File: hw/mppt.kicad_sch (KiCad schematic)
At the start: 11 parts

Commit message: hw changes
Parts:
- TJ302, TJ303: footprint mppt:1225_SMD -> footprints:1225_SMD
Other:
- moved on the sheet: TJ302, TJ303

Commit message: v0.2.0
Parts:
- removed TJ302 (x2): Thermal Jumper, Resistor_SMD:R_0805_2012Metric, symbol Jumper:SolderJumper_2_Bridged
- removed TJ302, TJ303: Thermal Jumper, footprints:1225_SMD, symbol Jumper:SolderJumper_2_Bridged
- H101, H102, H103, H104: footprint MountingHole:MountingHole_3.5mm -> MountingHole:MountingHole_3.2mm_M3
- TJ303: footprint footprints:1225_SMD -> footprints:vishay_THJP1225ABT1; Cost 2.60 -> 2.03; P/N 71-THJP1225AST1 -> THJP1225ABT1
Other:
- added sheet comm_can (comm_can.kicad_sch)
- sheet controller ports: added CAN_RX, CAN_TX; removed none
- note added: "v0.1.1 - Fix for BNC footprint swapping signal and ground. - Fix for OPA990 footprint, rotating three pins. - Fix for mislabeling 1uF 2220 switching cap. This should be 2.2uF. - Fix for bad ground isolation for current sensors. - Fix for ERROR LED being hooked up to USB_DP and CAN1_TD pin. v0.2.0rc (summer array testing) - Revised component symbol->footprint->model listings. - Updated component s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"
- note added: "v0.2.0rc"
- note removed: "v0.1.1rc"
- note removed: "v0.1.1rc - Fix for BNC footprint swapping signal and ground. - Fix for OPA990 footprint, rotating three pins. - Fix for mislabeling 1uF 2220 switching cap. This should be 2.2uF. - Fix for bad ground isolation for current sensors. - Fix for ERROR LED being hooked up to USB_DP and CAN1_TD pin. v0.2.0 (summer array testing) - Swap mounting holes to M3. - Add I/O power fuse. - Add HF low uF caps on I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"
- company: UT LHR Solar -> LHR Solar
- moved on the sheet: TJ303

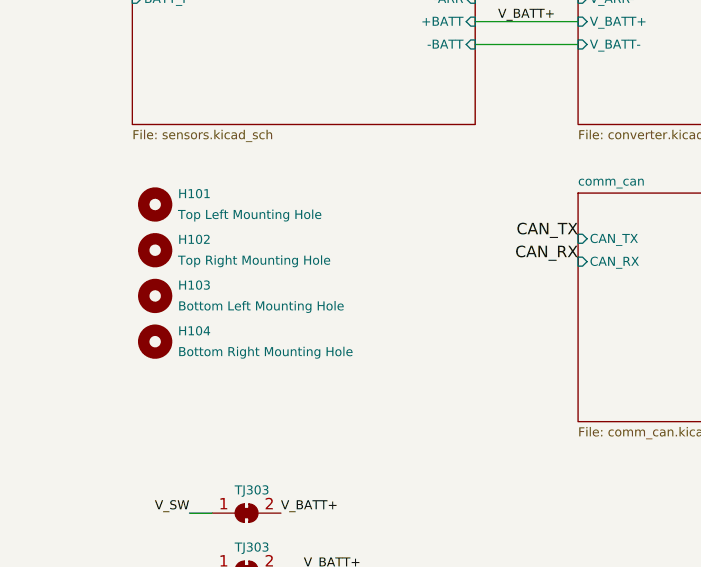
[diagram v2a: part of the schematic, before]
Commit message: bugfix for wrong adc pin for batt current measurements
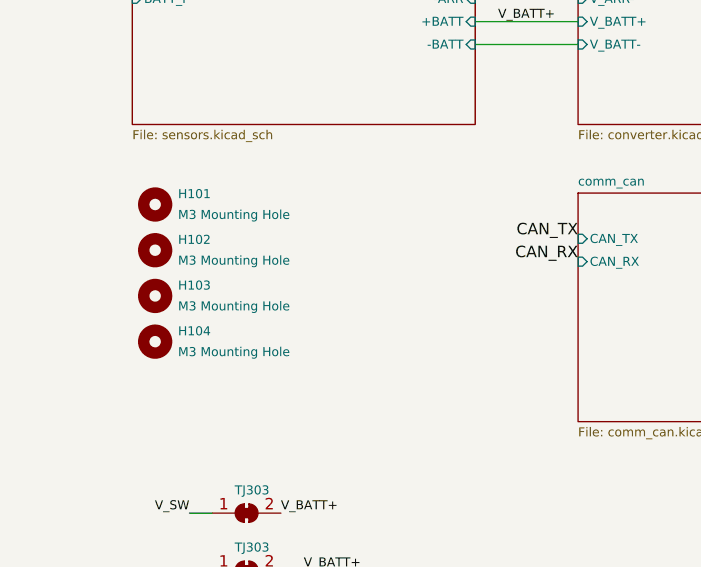
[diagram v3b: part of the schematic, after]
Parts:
- H101: value Top Left Mounting Hole -> M3 Mounting Hole
- H102: value Top Right Mounting Hole -> M3 Mounting Hole
- H103: value Bottom Left Mounting Hole -> M3 Mounting Hole
- H104: value Bottom Right Mounting Hole -> M3 Mounting Hole
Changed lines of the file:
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@@
       (effects (font (size 1 1)) (justify left))
     )
-    (property "Value" "Top Left Mounting Hole" (at 39.37 102.743 0)
+    (property "Value" "M3 Mounting Hole" (at 39.37 102.743 0)
       (effects (font (size 1 1)) (justify left))
     )
@@
       (effects (font (size 1 1)) (justify left))
     )
-    (property "Value" "Bottom Left Mounting Hole" (at 39.37 112.903 0)
+    (property "Value" "M3 Mounting Hole" (at 39.37 112.903 0)
       (effects (font (size 1 1)) (justify left))
     )
@@
       (effects (font (size 1 1)) (justify left))
     )
-    (property "Value" "Top Right Mounting Hole" (at 39.37 107.823 0)
+    (property "Value" "M3 Mounting Hole" (at 39.37 107.823 0)
       (effects (font (size 1 1)) (justify left))
     )
@@
       (effects (font (size 1 1)) (justify left))
     )
-    (property "Value" "Bottom Right Mounting Hole" (at 39.37 117.983 0)
+    (property "Value" "M3 Mounting Hole" (at 39.37 117.983 0)
       (effects (font (size 1 1)) (justify left))
     )

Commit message: v3 savestate
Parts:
- removed TJ303 (x3): Thermal Jumper, footprints:vishay_THJP1225ABT1, symbol Jumper:SolderJumper_2_Bridged
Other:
- added sheet power_reg (power_reg.kicad_sch)
- note added: "v0.1.1 - Fix for BNC footprint swapping signal and ground. - Fix for OPA990 footprint, rotating three pins. - Fix for mislabeling 1uF 2220 switching cap. This should be 2.2uF. - Fix for bad ground isolation for current sensors. - Fix for ERROR LED being hooked up to USB_DP and CAN1_TD pin. v0.2.0 - Revised component symbol->footprint->model listings. - Updated component suppliers. - Swapped mount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"
- note added: "v0.3.0rc"
- note removed: "v0.1.1 - Fix for BNC footprint swapping signal and ground. - Fix for OPA990 footprint, rotating three pins. - Fix for mislabeling 1uF 2220 switching cap. This should be 2.2uF. - Fix for bad ground isolation for current sensors. - Fix for ERROR LED being hooked up to USB_DP and CAN1_TD pin. v0.2.0rc (summer array testing) - Revised component symbol->footprint->model listings. - Updated component s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"
- note removed: "v0.2.0rc"
- moved on the sheet: H101, H102, H103, H104

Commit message: savestate
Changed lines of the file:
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@@
     (effects (font (size 2 2) (thickness 0.4) bold) (justify left bottom))
   )
-  (text "v0.1.1\n- Fix for BNC footprint swapping signal and ground.\n- Fix for OPA990 footprint, rotating three pins.\n- Fix for mislabeling 1uF 2220 switching cap. This should be 2.2uF.\n- Fix for bad ground isolation for current sensors.\n- Fix for ERROR LED being hooked up to USB_DP and CAN1_TD pin.\n\nv0.2.0\n- Revised component symbol->footprint->model listings.\n- Updated component suppliers.\n- Swapped mounting holes to M3.\n- Added I/O power fuse.\n- Swapped I/O connectors to XT60PW.\n- Removed heatsink and some thermal jumpers.\n- Added HF low uF caps on I/O to remove switching noise.\n- Added CAN circuitry.\n- Removed BNC.\n\nv0.3.0rc\n- Modify converter design based on automation improvements and updated\n  design specifications.\n- RTD/PTC thermistors on switches, inductor.\n\nv0.4.0 (final MPPT version)\n- Convert STM32 Nucleo to bare chip.\n- Isolated 12V/12V regulator. 12V to 5V regulator, 5V to 3V3 regulator.\n- Hit board size, cost target of 75x50 mm^{2}, <75$/board.\n"
-    (at 176.53 90.17 0)
+  (text "v0.1.1\n- Fix for BNC footprint swapping signal and ground.\n- Fix for OPA990 footprint, rotating three pins.\n- Fix for mislabeling 1uF 2220 switching cap. This should be 2.2uF.\n- Fix for bad ground isolation for current sensors.\n- Fix for ERROR LED being hooked up to USB_DP and CAN1_TD pin.\n\nv0.2.0\n- Revised component symbol->footprint->model listings.\n- Updated component suppliers.\n- Swapped mounting holes to M3.\n- Added I/O power fuse.\n- Swapped I/O connectors to XT60PW.\n- Removed heatsink and some thermal jumpers.\n- Added HF low uF caps on I/O to remove switching noise.\n- Added CAN circuitry.\n- Removed BNC.\n\nv0.3.0rc\n- Convert STM32 Nucleo to bare chip.\n- Isolated 12V/12V regulator. 12V to 5V regulator, 5V to 3V3 regulator.\n- Digital eFuse input.\n- Removed another thermal jumper.\n- RTD/PTC thermistors on switches, inductor.\n- Hit board size, cost target of 75x50 mm^{2}, <75$/board.\n"
+    (at 176.53 85.09 0)
     (effects (font (size 1 1)) (justify left bottom))
   )
